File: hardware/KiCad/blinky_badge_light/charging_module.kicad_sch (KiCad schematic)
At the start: 15 parts, among them Q1 N-Channel MOSFET, Q3 N-Channel MOSFET, U2 TP4056

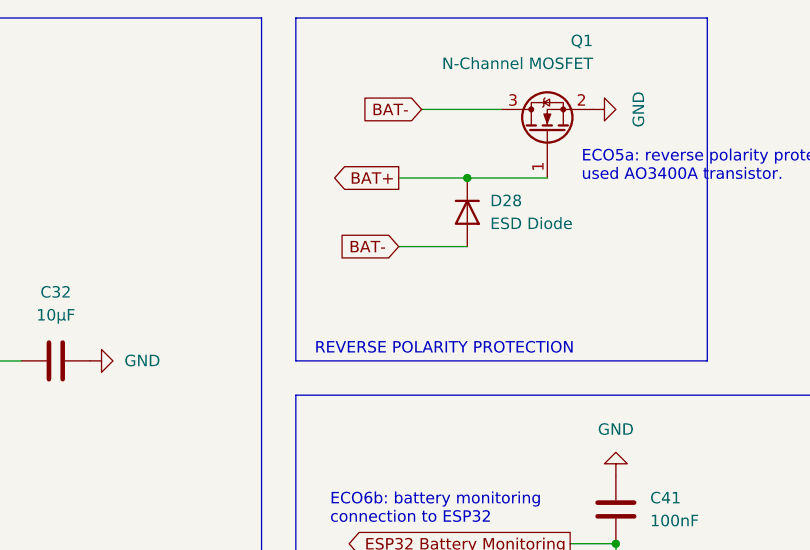
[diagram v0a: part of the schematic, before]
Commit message: change reverse battery protection circuit so diode goes to ground
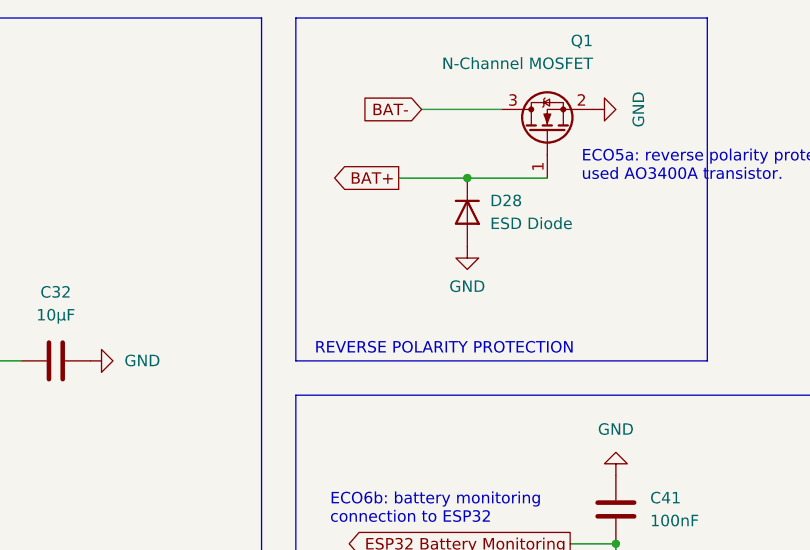
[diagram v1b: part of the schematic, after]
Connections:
- net BAT-: no longer D28.2 (A)
- net GND: now also D28.2 (A)
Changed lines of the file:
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@@
-	(wire
-		(pts
-			(xy 168.91 41.91) (xy 176.53 41.91)
-		)
-		(stroke
-			(width 0)
-			(type default)
-		)
-	)
 	(wire
 		(pts
@@
 		(property "Intersheetrefs" "${INTERSHEET_REFS}"
 			(at 171.5497 95.25 0)
-			(effects
-				(font
-					(size 1.27 1.27)
-				)
-				(justify right)
-				(hide yes)
-			)
-		)
-	)
-	(global_label "BAT-"
-		(shape input)
-		(at 168.91 41.91 180)
-		(fields_autoplaced yes)
-		(effects
-			(font
-				(size 1.27 1.27)
-			)
-			(justify right)
-		)
-		(property "Intersheetrefs" "${INTERSHEET_REFS}"
-			(at 161.0262 41.91 0)
 			(effects
 				(font
@@
 					(unit 1)
 				)
+			)
+		)
+	)
+	(symbol
+		(lib_id "power:GND")
+		(at 176.53 41.91 0)
+		(unit 1)
+		(exclude_from_sim no)
+		(in_bom yes)
+		(on_board yes)
+		(dnp no)
+		(fields_autoplaced yes)
+		(property "Reference" "#PWR039"
+			(at 176.53 48.26 0)
+			(effects
+				(font
+					(size 1.27 1.27)
+				)
+				(hide yes)
+			)
+		)
+		(property "Value" "GND"
+			(at 176.53 46.355 0)
+			(effects
+				(font
+					(size 1.27 1.27)
+				)
+			)
+		)
+		(property "Footprint" ""
+			(at 176.53 41.91 0)
+			(effects
+				(font
+					(size 1.27 1.27)
+				)
+				(hide yes)
+			)
+		)
+		(property "Datasheet" ""
+			(at 176.53 41.91 0)
+			(effects
+				(font
+					(size 1.27 1.27)
+				)
+				(hide yes)
+			)
+		)
+		(property "Description" "Power symbol creates a global label with name \"GND\" , ground"
+			(at 176.53 41.91 0)
+			(effects
+				(font
+					(size 1.27 1.27)
+				)
+				(hide yes)
+			)
+		)
+		(pin "1"
+		)
+		(instances
+			(project ""
+				(path "/f33039b1-b38b-4cb6-baf0-07a137773378/ff49f689-50f6-47c9-b665-80ddb7cbc42d"
+					(reference "#PWR039")
+					(unit 1)
+				)

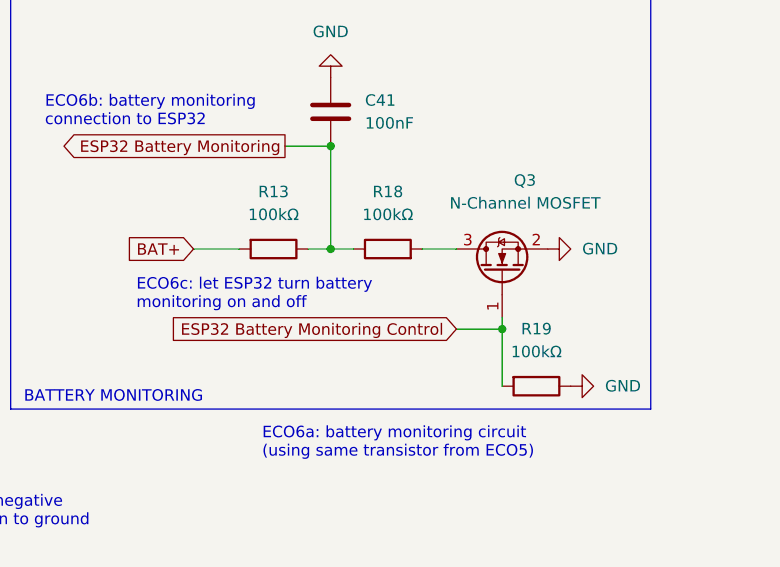
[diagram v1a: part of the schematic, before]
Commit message: update battery protection circuit and draw routes
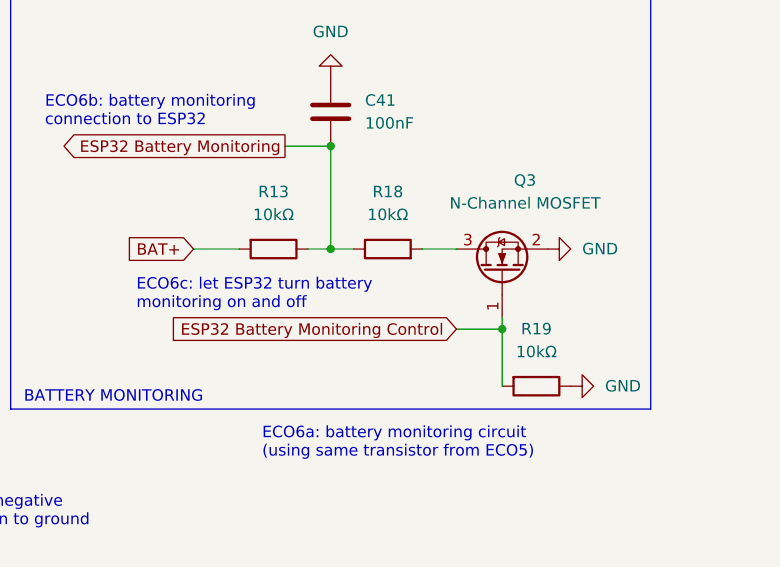
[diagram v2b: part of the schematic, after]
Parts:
- R13, R18, R19: value 100kΩ -> 10kΩ; JLCPCB Part # C25803 -> C25804
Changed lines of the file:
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@@
 			)
 		)
-		(property "Value" "100kΩ"
+		(property "Value" "10kΩ"
 			(at 186.69 82.55 90)
 			(effects
@@
 			)
 		)
-		(property "Datasheet" "https://jlcpcb.com/api/file/downloadByFileSystemAccessId/8579706350726930432"
+		(property "Datasheet" "https://jlcpcb.com/api/file/downloadByFileSystemAccessId/8579706381320323072"
 			(at 186.69 86.36 0)
 			(effects
@@
 			)
 		)
-		(property "JLCPCB Part #" "C25803"
+		(property "JLCPCB Part #" "C25804"
 			(at 186.69 86.36 90)
 			(effects
@@
 			)
 		)
-		(property "Value" "100kΩ"
+		(property "Value" "10kΩ"
 			(at 215.9 97.79 90)
 			(effects
@@
 			)
 		)
-		(property "Datasheet" "https://jlcpcb.com/api/file/downloadByFileSystemAccessId/8579706350726930432"
+		(property "Datasheet" "https://jlcpcb.com/api/file/downloadByFileSystemAccessId/8579706381320323072"
 			(at 215.9 101.6 0)
 			(effects
@@
 			)
 		)
-		(property "JLCPCB Part #" "C25803"
+		(property "JLCPCB Part #" "C25804"
 			(at 215.9 101.6 90)
 			(effects
@@
 			)
 		)
-		(property "Value" "100kΩ"
+		(property "Value" "10kΩ"
 			(at 199.39 82.55 90)
 			(effects
@@
 			)
 		)
-		(property "Datasheet" "https://jlcpcb.com/api/file/downloadByFileSystemAccessId/8579706350726930432"
+		(property "Datasheet" "https://jlcpcb.com/api/file/downloadByFileSystemAccessId/8579706381320323072"
 			(at 199.39 86.36 0)
 			(effects
@@
 			)
 		)
-		(property "JLCPCB Part #" "C25803"
+		(property "JLCPCB Part #" "C25804"
 			(at 199.39 86.36 90)
 			(effects

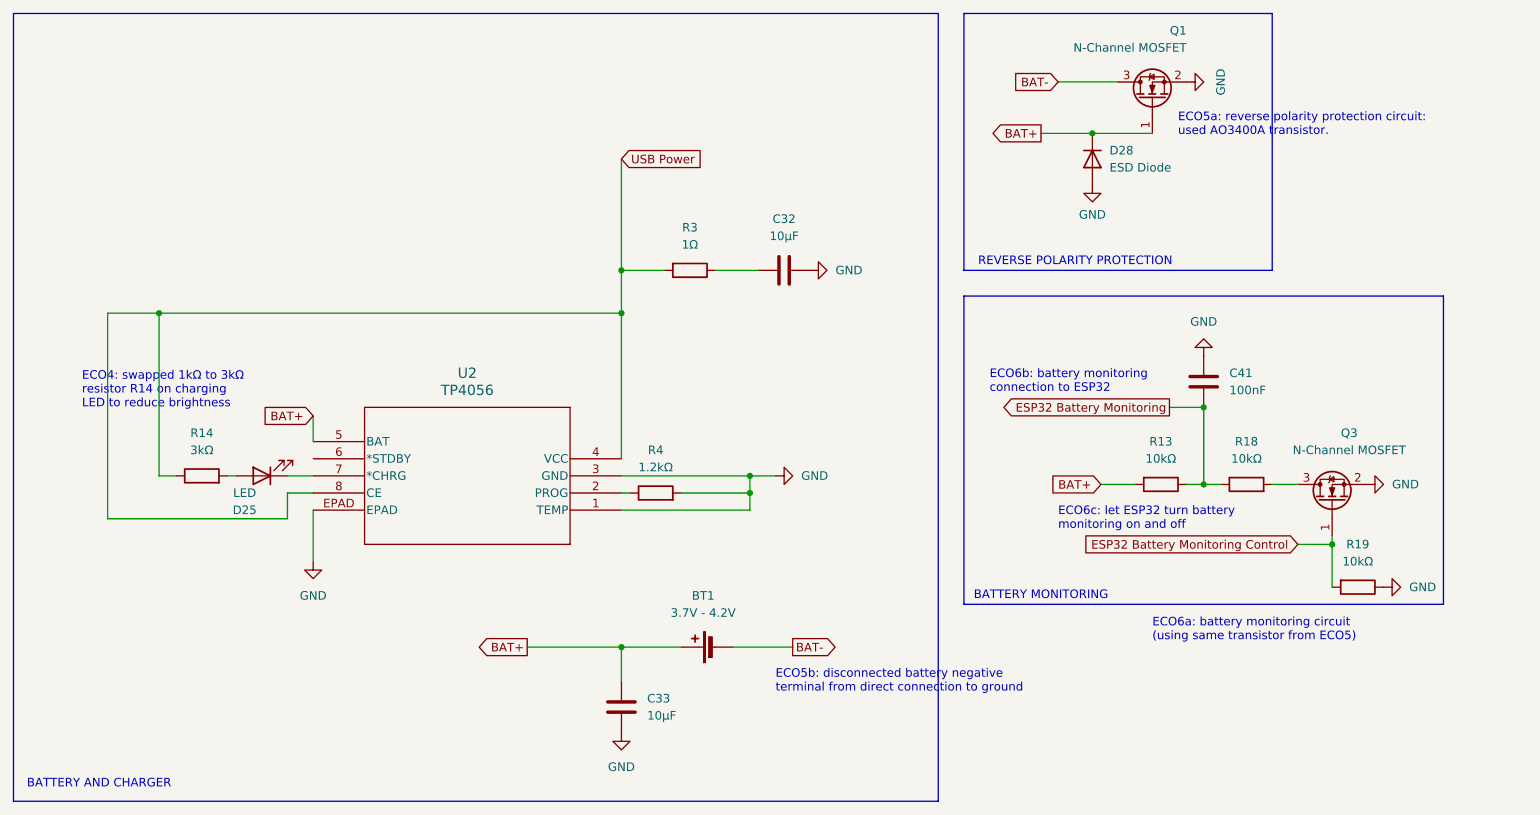
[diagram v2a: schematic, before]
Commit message: remove text from review
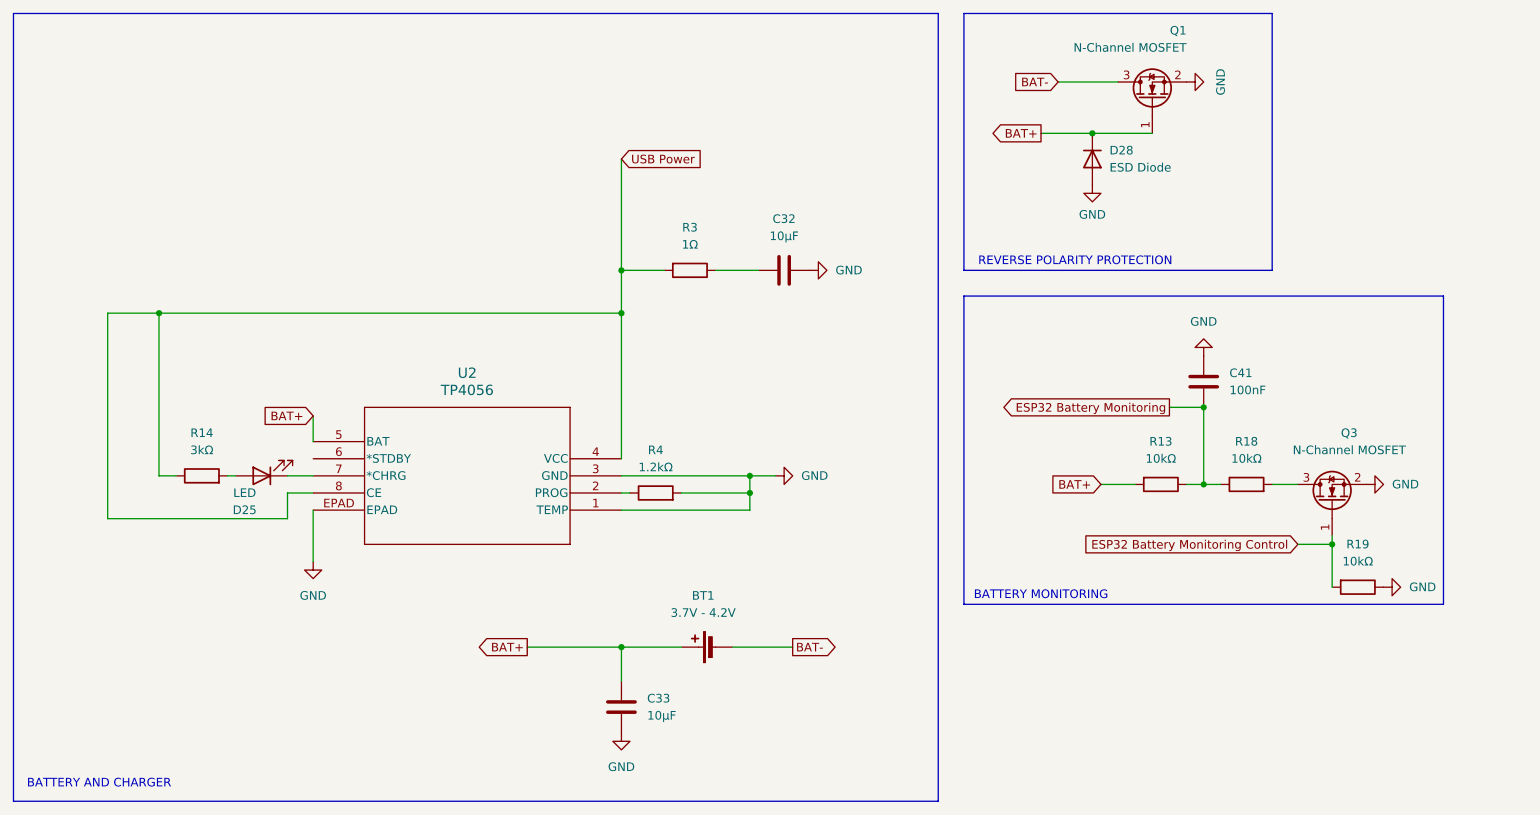
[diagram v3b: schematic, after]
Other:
- note removed: "ECO4: swapped 1kΩ to 3kΩ resistor R14 on charging LED to reduce brightness"
- note removed: "ECO5a: reverse polarity protection circuit: used AO3400A transistor."
- note removed: "ECO5b: disconnected battery negative terminal from direct connection to ground"
- note removed: "ECO6a: battery monitoring circuit (using same transistor from ECO5)"
- note removed: "ECO6b: battery monitoring connection to ESP32"
- note removed: "ECO6c: let ESP32 turn battery monitoring on and off"
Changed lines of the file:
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@@
-		)
-	)
-	(text "ECO5a: reverse polarity protection circuit:\nused AO3400A transistor."
-		(exclude_from_sim yes)
-		(at 189.23 33.02 0)
-		(effects
-			(font
-				(size 1.27 1.27)
-				(color 119 0 255 1)
-			)
-			(justify left)
-		)
-	)
-	(text "ECO5b: disconnected battery negative\nterminal from direct connection to ground"
-		(exclude_from_sim yes)
-		(at 129.54 115.57 0)
-		(effects
-			(font
-				(size 1.27 1.27)
-				(color 119 0 255 1)
-			)
-			(justify left)
-		)
-	)
-	(text "ECO6c: let ESP32 turn battery\nmonitoring on and off"
-		(exclude_from_sim yes)
-		(at 171.45 91.44 0)
-		(effects
-			(font
-				(size 1.27 1.27)
-				(color 119 0 255 1)
-			)
-			(justify left)
-		)
-	)
-	(text "ECO4: swapped 1kΩ to 3kΩ \nresistor R14 on charging \nLED to reduce brightness"
-		(exclude_from_sim yes)
-		(at 26.67 72.39 0)
-		(effects
-			(font
-				(size 1.27 1.27)
-				(color 119 0 255 1)
-			)
-			(justify left)
-		)
-	)
-	(text "ECO6b: battery monitoring\nconnection to ESP32"
-		(exclude_from_sim yes)
-		(at 161.29 71.12 0)
-		(effects
-			(font
-				(size 1.27 1.27)
-				(color 119 0 255 1)
-			)
-			(justify left)
 		)
 	)
@@
 		)
 	)
-	(text "ECO6a: battery monitoring circuit\n(using same transistor from ECO5)"
-		(exclude_from_sim yes)
-		(at 185.42 107.95 0)
-		(effects
-			(font
-				(size 1.27 1.27)
-				(color 119 0 255 1)
-			)
-			(justify left)
-		)
-	)

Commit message: fixing a couple things and exported files
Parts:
- Q1: JLCBCB Part # C20917 -> (none); JLCPCB Part # (none) -> C20917
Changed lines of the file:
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@@
 			)
 		)
-		(property "JLCBCB Part #" "C20917"
+		(property "JLCPCB Part #" "C20917"
 			(at 185.42 29.21 0)
 			(effects

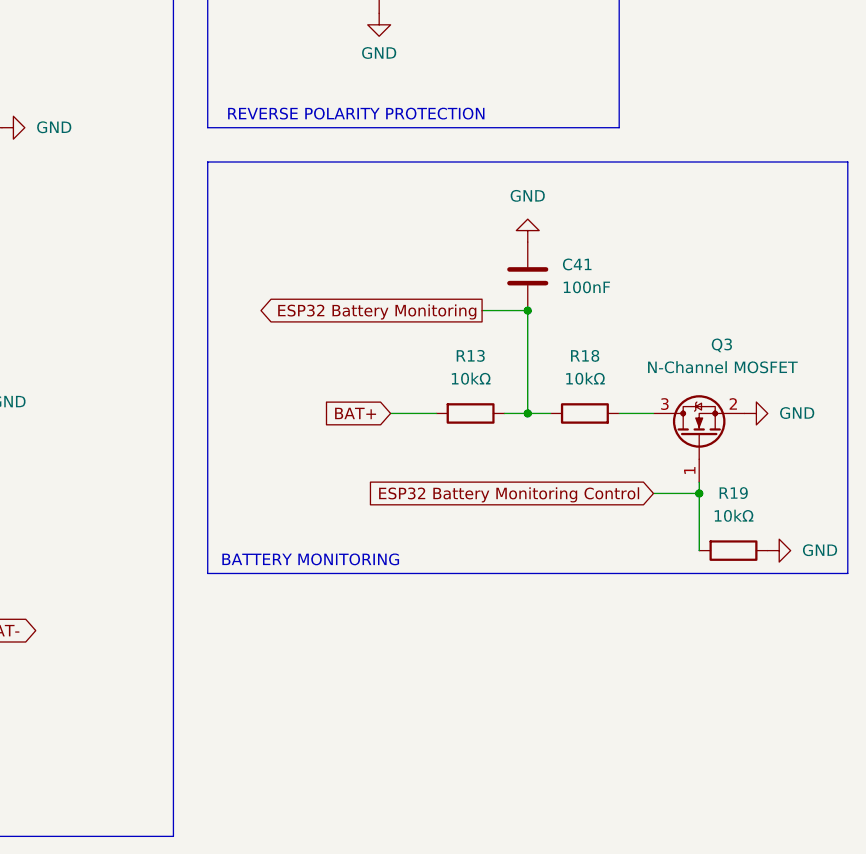
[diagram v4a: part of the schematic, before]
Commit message: added new transistor and resistor to battery monitoring circuit, adjusted two leds/capacitors position slightly
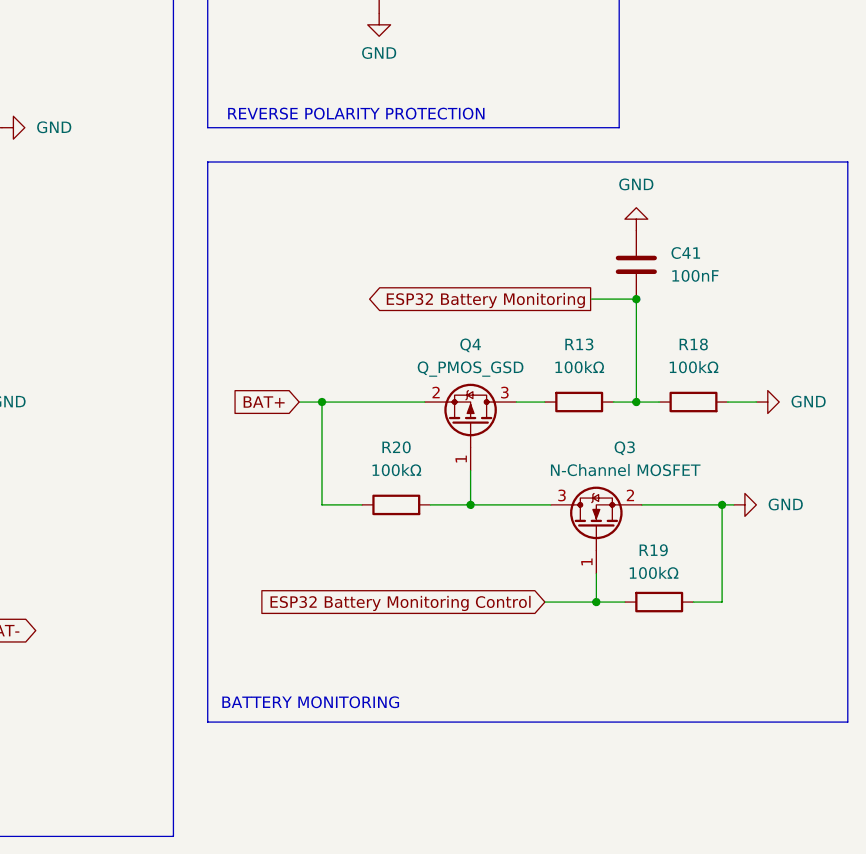
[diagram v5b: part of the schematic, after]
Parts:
- added Q4: Q_PMOS_GSD, Package_TO_SOT_SMD:SOT-23, symbol Device:Q_PMOS_GSD
- added R20: 100kΩ, Resistor_SMD:R_0603_1608Metric, symbol Device:R
- R13, R18, R19: value 10kΩ -> 100kΩ; JLCPCB Part # C25804 -> C25803
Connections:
- net BAT+: now also Q4.2 (S), R20.1; no longer R13.2
- net GND: now also R18.2
- net at Q3.3 (D): now also Q4.1 (G), R20.2; no longer R18.2
- new net: Q4.3 (D), R13.2
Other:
- moved on the sheet: C41, Q3, R13, R18, R19

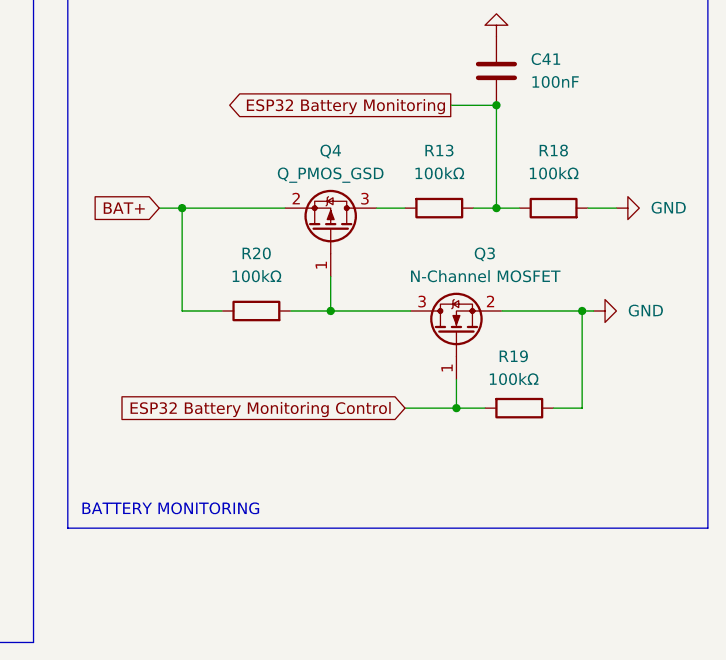
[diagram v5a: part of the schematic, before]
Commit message: changed resistors on battery monitoring (back) to 10k
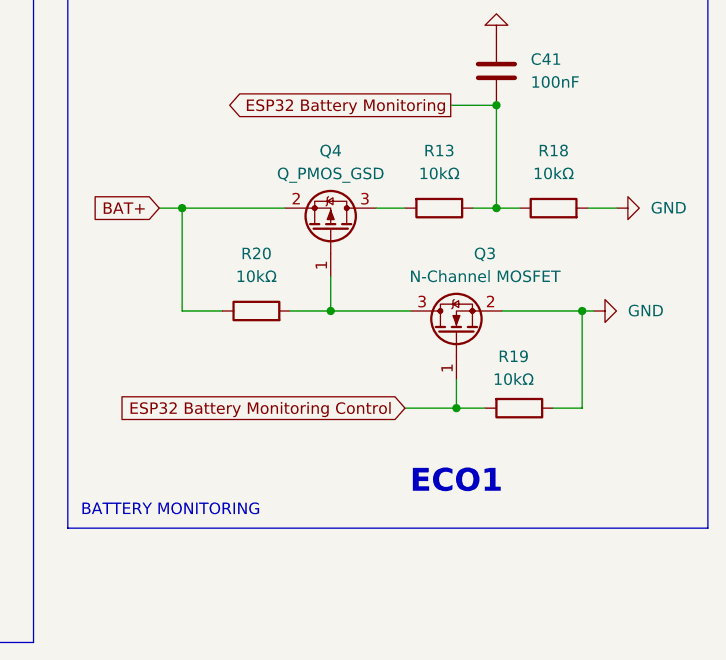
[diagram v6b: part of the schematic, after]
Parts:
- R13, R18, R19, R20: value 100kΩ -> 10kΩ; JLCPCB Part # C25803 -> C25804
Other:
- note added: "ECO1"
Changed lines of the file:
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@@
+		)
+	)
+	(text "ECO1"
+		(exclude_from_sim yes)
+		(at 200.66 115.57 0)
+		(effects
+			(font
+				(face "KiCad Font")
+				(size 2.54 2.54)
+				(thickness 0.508)
+				(bold yes)
+				(color 137 36 255 1)
+			)
 		)
 	)
@@
 			)
 		)
-		(property "Value" "100kΩ"
+		(property "Value" "10kΩ"
 			(at 198.755 81.28 90)
 			(effects
@@
 			)
 		)
-		(property "Datasheet" "https://jlcpcb.com/api/file/downloadByFileSystemAccessId/8579706350726930432"
+		(property "Datasheet" "https://jlcpcb.com/api/file/downloadByFileSystemAccessId/8579706381320323072"
 			(at 198.755 85.09 0)
 			(effects
@@
 			)
 		)
-		(property "JLCPCB Part #" "C25803"
+		(property "JLCPCB Part #" "C25804"
 			(at 198.755 85.09 90)
 			(effects
@@
 			)
 		)
-		(property "Value" "100kΩ"
+		(property "Value" "10kΩ"
 			(at 207.01 104.14 90)
 			(effects
@@
 			)
 		)
-		(property "Datasheet" "https://jlcpcb.com/api/file/downloadByFileSystemAccessId/8579706350726930432"
+		(property "Datasheet" "https://jlcpcb.com/api/file/downloadByFileSystemAccessId/8579706381320323072"
 			(at 207.645 107.315 0)
 			(effects
@@
 			)
 		)
-		(property "JLCPCB Part #" "C25803"
+		(property "JLCPCB Part #" "C25804"
 			(at 207.645 107.315 90)
 			(effects
@@
 			)
 		)
-		(property "Value" "100kΩ"
+		(property "Value" "10kΩ"
 			(at 211.455 81.28 90)
 			(effects
@@
 			)
 		)
-		(property "Datasheet" "https://jlcpcb.com/api/file/downloadByFileSystemAccessId/8579706350726930432"
+		(property "Datasheet" "https://jlcpcb.com/api/file/downloadByFileSystemAccessId/8579706381320323072"
 			(at 211.455 85.09 0)
 			(effects
@@
 			)
 		)
-		(property "JLCPCB Part #" "C25803"
+		(property "JLCPCB Part #" "C25804"
 			(at 211.455 85.09 90)
 			(effects
@@
 			)
 		)
-		(property "Value" "100kΩ"
+		(property "Value" "10kΩ"
 			(at 178.435 92.71 90)
 			(effects
@@
 			)
 		)
-		(property "Datasheet" "https://jlcpcb.com/api/file/downloadByFileSystemAccessId/8579706350726930432"
+		(property "Datasheet" "https://jlcpcb.com/api/file/downloadByFileSystemAccessId/8579706381320323072"
 			(at 178.435 96.52 0)
 			(effects
@@
 			)
 		)
-		(property "JLCPCB Part #" "C25803"
+		(property "JLCPCB Part #" "C25804"
 			(at 178.435 96.52 90)
 			(effects
